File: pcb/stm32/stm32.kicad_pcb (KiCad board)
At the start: 2 copper layers, 57 parts, among them J1 Conn_01x02_Pin, J10 4P4C, J11 4P4C, J12 4P4C, J13 Conn_01x02_Pin, J14 4P4C, J15 4P4C, J16 USB_C_Receptacle, J2 Conn_01x02_Pin, J3 Conn_02x05_Top_Bottom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

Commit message: PCB updates
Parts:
- added Q2: DMG3415, Package_TO_SOT_SMD:SOT-23, F.Cu at (215.0, 53.3)
- added U10: TPL5110, Package_TO_SOT_SMD:SOT-23-6, F.Cu at (215.1, 48.9)
- moved BT1 5.80 mm to (116.8, 40.6)

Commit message: PCB in progress
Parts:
- moved J9 151.8 mm to (50.8, 137.2)
- moved U6 147.4 mm to (72.2, 52.7)
- moved Q1 144.0 mm to (74.6, 61.9)
- moved F1 140.7 mm to (66.0, 63.5)
- moved L1 136.9 mm to (72.2, 47.8)
- moved J10 130.6 mm to (68.7, 137.2)
- moved C7 125.1 mm to (69.4, 53.2), turned to -90 degrees
- moved R14 116.6 mm to (91.4, 33.0)
- moved J16 113.4 mm to (61.0, 81.3), turned to -90 degrees
- moved U8 112.9 mm to (70.0, 82.9)
- moved U9 111.6 mm to (71.8, 78.1)
- moved R15 108.5 mm to (94.0, 38.1)
- moved J11 106.8 mm to (86.9, 137.2)
- moved U4 102.9 mm to (132.1, 71.1)
- moved J12 83.2 mm to (104.6, 136.9)
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
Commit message: Progress
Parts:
- moved C1 173.1 mm to (84.2, 40.6)
- moved U7 154.8 mm to (87.9, 104.0)
- moved U5 153.8 mm to (53.3, 116.8)
- moved J13 142.4 mm to (76.2, 33.6)
- moved U3 129.5 mm to (114.3, 101.6)
- moved C2 122.6 mm to (121.0, 106.7)
- moved C3 117.3 mm to (126.0, 106.7)
- moved C8 115.0 mm to (78.7, 63.5), turned to 90 degrees
- moved Q2 112.7 mm to (102.6, 61.9)
- moved U10 112.7 mm to (102.7, 57.5)
- moved R11 104.0 mm to (100.1, 35.6)
- moved C10 97.4 mm to (105.7, 36.0)
- moved C9 97.4 mm to (105.7, 33.0)
- moved R12 78.0 mm to (120.5, 70.4)
- moved R13 78.0 mm to (120.5, 73.7)
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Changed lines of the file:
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@@
   )
   (footprint "Resistor_SMD:R_1206_3216Metric" (layer "F.Cu")
-    (at 198.44 72.87)
+    (at 120.4575 70.37)
     (descr "Resistor SMD 1206 (3216 Metric), square (rectangular) end terminal, IPC_7351 nominal, (Body size source: IPC-SM-782 page 72, https://www.pcb-3d.com/wordpress/wp-content/uploads/ipc-sm-782a_amendment_1_and_2.pdf), generated with kicad-footprint-generator")
     (tags "resistor")
@@
   )
   (footprint "Capacitor_SMD:C_0805_2012Metric" (layer "F.Cu")
-    (at 243.03 95.39)
+    (at 120.97 106.68)
     (descr "Capacitor SMD 0805 (2012 Metric), square (rectangular) end terminal, IPC_7351 nominal, (Body size source: IPC-SM-782 page 76, https://www.pcb-3d.com/wordpress/wp-content/uploads/ipc-sm-782a_amendment_1_and_2.pdf, https://docs.google.com/spreadsheets/d/1BsfQQcO9C6DZCsRaXUlFlo91Tg2WpOkGARC1WS5S8t0/edit?usp=sharing), generated with kicad-footprint-generator")
     (tags "capacitor")
@@
   )
   (footprint "Package_TO_SOT_SMD:SOT-23" (layer "F.Cu")
-    (at 74.5975 61.91)
+    (at 74.5975 63.5)
     (descr "SOT, 3 Pin (https://www.jedec.org/system/files/docs/to-236h.pdf variant AB), generated with kicad-footprint-generator ipc_gullwing_generator.py")
     (tags "SOT TO_SOT_SMD")
@@
   )
   (footprint "Capacitor_SMD:C_0805_2012Metric" (layer "F.Cu")
-    (at 243.03 98.4)
+    (at 126.05 106.68)
     (descr "Capacitor SMD 0805 (2012 Metric), square (rectangular) end terminal, IPC_7351 nominal, (Body size source: IPC-SM-782 page 76, https://www.pcb-3d.com/wordpress/wp-content/uploads/ipc-sm-782a_amendment_1_and_2.pdf, https://docs.google.com/spreadsheets/d/1BsfQQcO9C6DZCsRaXUlFlo91Tg2WpOkGARC1WS5S8t0/edit?usp=sharing), generated with kicad-footprint-generator")
     (tags "capacitor")
@@
   )
   (footprint "Package_TO_SOT_SMD:SOT-23" (layer "F.Cu")
-    (at 214.9625 53.34)
+    (at 102.6075 61.92)
     (descr "SOT, 3 Pin (https://www.jedec.org/system/files/docs/to-236h.pdf variant AB), generated with kicad-footprint-generator ipc_gullwing_generator.py")
     (tags "SOT TO_SOT_SMD")
@@
   )
   (footprint "Capacitor_SMD:C_0805_2012Metric" (layer "F.Cu")
-    (at 193.41 72.45)
+    (at 78.74 63.5 90)
     (descr "Capacitor SMD 0805 (2012 Metric), square (rectangular) end terminal, IPC_7351 nominal, (Body size source: IPC-SM-782 page 76, https://www.pcb-3d.com/wordpress/wp-content/uploads/ipc-sm-782a_amendment_1_and_2.pdf, https://docs.google.com/spreadsheets/d/1BsfQQcO9C6DZCsRaXUlFlo91Tg2WpOkGARC1WS5S8t0/edit?usp=sharing), generated with kicad-footprint-generator")
     (tags "capacitor")
@@
     (property "ki_keywords" "cap capacitor")
     (attr smd)
-    (fp_text reference "C8" (at 0 -1.68) (layer "F.SilkS")
+    (fp_text reference "C8" (at 2.54 0 180) (layer "F.SilkS")
         (effects (font (size 1 1) (thickness 0.15)))
     )
-    (fp_text value "10u" (at 0 1.68) (layer "F.Fab")
+    (fp_text value "10u" (at -2.54 0 180) (layer "F.Fab")
         (effects (font (size 1 1) (thickness 0.15)))
     )
-    (fp_text user "${REFERENCE}" (at 0 0) (layer "F.Fab")
+    (fp_text user "${REFERENCE}" (at 0 0 90) (layer "F.Fab")
         (effects (font (size 0.5 0.5) (thickness 0.08)))
     )
@@
     (fp_line (start 1 0.625) (end -1 0.625)
       (stroke (width 0.1) (type solid)) (layer "F.Fab"))
-    (pad "1" smd roundrect (at -0.95 0) (size 1 1.45) (layers "F.Cu" "F.Paste" "F.Mask") (roundrect_rratio 0.25)
+    (pad "1" smd roundrect (at -0.95 0 90) (size 1 1.45) (layers "F.Cu" "F.Paste" "F.Mask") (roundrect_rratio 0.25)
       (net 3 "+3.3V") (pintype "passive"))
-    (pad "2" smd roundrect (at 0.95 0) (size 1 1.45) (layers "F.Cu" "F.Paste" "F.Mask") (roundrect_rratio 0.25)
+    (pad "2" smd roundrect (at 0.95 0 90) (size 1 1.45) (layers "F.Cu" "F.Paste" "F.Mask") (roundrect_rratio 0.25)
       (net 2 "GND") (pintype "passive"))
     (model "${KICAD6_3DMODEL_DIR}/Capacitor_SMD.3dshapes/C_0805_2012Metric.wrl"
@@
   )
   (footprint "Connector_PinHeader_2.00mm:PinHeader_1x02_P2.00mm_Vertical" (layer "F.Cu")
-    (at 213.88 69.96)
+    (at 76.2 33.56)
     (descr "Through hole straight pin header, 1x02, 2.00mm pitch, single row")
     (tags "Through hole pin header THT 1x02 2.00mm single row")
@@
   )
   (footprint "Capacitor_SMD:C_0805_2012Metric" (layer "F.Cu")
-    (at 193.41 75.46)
+    (at 105.73 33.02)
     (descr "Capacitor SMD 0805 (2012 Metric), square (rectangular) end terminal, IPC_7351 nominal, (Body size source: IPC-SM-782 page 76, https://www.pcb-3d.com/wordpress/wp-content/uploads/ipc-sm-782a_amendment_1_and_2.pdf, https://docs.google.com/spreadsheets/d/1BsfQQcO9C6DZCsRaXUlFlo91Tg2WpOkGARC1WS5S8t0/edit?usp=sharing), generated with kicad-footprint-generator")
     (tags "capacitor")
@@
   )
   (footprint "Capacitor_SMD:C_0805_2012Metric" (layer "F.Cu")
-    (at 193.41 78.47)
+    (at 105.73 36.03)
     (descr "Capacitor SMD 0805 (2012 Metric), square (rectangular) end terminal, IPC_7351 nominal, (Body size source: IPC-SM-782 page 76, https://www.pcb-3d.com/wordpress/wp-content/uploads/ipc-sm-782a_amendment_1_and_2.pdf, https://docs.google.com/spreadsheets/d/1BsfQQcO9C6DZCsRaXUlFlo91Tg2WpOkGARC1WS5S8t0/edit?usp=sharing), generated with kicad-footprint-generator")
     (tags "capacitor")
@@
   )
   (footprint "Package_TO_SOT_SMD:SOT-23-5" (layer "F.Cu")
-    (at 243.38 91.66)
+    (at 114.3 101.6)
     (descr "SOT, 5 Pin (https://www.jedec.org/sites/default/files/docs/Mo-178c.PDF variant AA), generated with kicad-footprint-generator ipc_gullwing_generator.py")
     (tags "SOT TO_SOT_SMD")
@@
   )
   (footprint "Package_LGA:Bosch_LGA-8_2.5x2.5mm_P0.65mm_ClockwisePinNumbering" (layer "F.Cu")
-    (at 242.74 103.97)
+    (at 87.925 103.97)
     (descr "LGA-8")
     (tags "lga land grid array")
@@
   )
   (footprint "Package_TO_SOT_SMD:SOT-23-5" (layer "F.Cu")
-    (at 243.38 87.21)
+    (at 247.5175 54.29)
     (descr "SOT, 5 Pin (https://www.jedec.org/sites/default/files/docs/Mo-178c.PDF variant AA), generated with kicad-footprint-generator ipc_gullwing_generator.py")
     (tags "SOT TO_SOT_SMD")
@@
   )
   (footprint "Capacitor_SMD:C_0201_0603Metric" (layer "F.Cu")
-    (at 247.18 98.89)
+    (at 84.165 40.64)
     (descr "Capacitor SMD 0201 (0603 Metric), square (rectangular) end terminal, IPC_7351 nominal, (Body size source: https://www.vishay.com/docs/20052/crcw0201e3.pdf), generated with kicad-footprint-generator")
     (tags "capacitor")
@@
   )
   (footprint "Resistor_SMD:R_1206_3216Metric" (layer "F.Cu")
-    (at 198.44 76.16)
+    (at 120.4575 73.66)
     (descr "Resistor SMD 1206 (3216 Metric), square (rectangular) end terminal, IPC_7351 nominal, (Body size source: IPC-SM-782 page 72, https://www.pcb-3d.com/wordpress/wp-content/uploads/ipc-sm-782a_amendment_1_and_2.pdf), generated with kicad-footprint-generator")
     (tags "resistor")
@@
   )
   (footprint "Package_SO:SOIC-8_3.9x4.9mm_P1.27mm" (layer "F.Cu")
-    (at 250.18 88.21)
+    (at 254.3175 55.29)
     (descr "SOIC, 8 Pin (JEDEC MS-012AA, https://www.analog.com/media/en/package-pcb-resources/package/pkg_pdf/soic_narrow-r/r_8.pdf), generated with kicad-footprint-generator ipc_gullwing_generator.py")
     (tags "SOIC SO")
@@
   )
   (footprint "Package_TO_SOT_SMD:SOT-23-6" (layer "F.Cu")
-    (at 215.0925 48.89)
+    (at 102.7375 57.47)
     (descr "SOT, 6 Pin (https://www.jedec.org/sites/default/files/docs/Mo-178c.PDF variant AB), generated with kicad-footprint-generator ipc_gullwing_generator.py")
     (tags "SOT TO_SOT_SMD")
@@
   )
   (footprint "Resistor_SMD:R_1206_3216Metric" (layer "F.Cu")
-    (at 198.44 69.58)
+    (at 100.1375 35.56)
     (descr "Resistor SMD 1206 (3216 Metric), square (rectangular) end terminal, IPC_7351 nominal, (Body size source: IPC-SM-782 page 72, https://www.pcb-3d.com/wordpress/wp-content/uploads/ipc-sm-782a_amendment_1_and_2.pdf), generated with kicad-footprint-generator")
     (tags "resistor")
@@
   )
   (footprint "Package_TO_SOT_THT:TO-92_Inline" (layer "F.Cu")
-    (at 184.66 36.71)
+    (at 53.34 116.84)
     (descr "TO-92 leads in-line, narrow, oval pads, drill 0.75mm (see NXP sot054_po.pdf)")
     (tags "to-92 sc-43 sc-43a sot54 PA33 transistor")

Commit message: Setup board
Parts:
- moved U9 3.63 mm to (74.3, 75.5)
- moved U8 3.63 mm to (72.5, 80.2)
- moved J16 2.64 mm to (61.0, 78.6)
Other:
- board outline added: 99.1 x 50.8 mm
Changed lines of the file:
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@@
   )
   (setup
+    (stackup
+      (layer "F.SilkS" (type "Top Silk Screen"))
+      (layer "F.Paste" (type "Top Solder Paste"))
+      (layer "F.Mask" (type "Top Solder Mask") (thickness 0.01))
+      (layer "F.Cu" (type "copper") (thickness 0.035))
+      (layer "dielectric 1" (type "core") (thickness 1.51) (material "FR4") (epsilon_r 4.5) (loss_tangent 0.02))
+      (layer "B.Cu" (type "copper") (thickness 0.035))
+      (layer "B.Mask" (type "Bottom Solder Mask") (thickness 0.01))
+      (layer "B.Paste" (type "Bottom Solder Paste"))
+      (layer "B.SilkS" (type "Bottom Silk Screen"))
+      (copper_finish "HAL SnPb")
+      (dielectric_constraints no)
+    )
     (pad_to_mask_clearance 0)
     (pcbplotparams
@@
   )
   (footprint "Package_TO_SOT_SMD:SOT-23-6" (layer "F.Cu")
-    (at 69.9825 82.87)
+    (at 72.475 80.23)
     (descr "SOT, 6 Pin (https://www.jedec.org/sites/default/files/docs/Mo-178c.PDF variant AB), generated with kicad-footprint-generator ipc_gullwing_generator.py")
     (tags "SOT TO_SOT_SMD")
@@
   )
   (footprint "Connector_USB:USB_C_Receptacle_Amphenol_12401548E4-2A" (layer "F.Cu")
-    (at 60.96 81.28 -90)
+    (at 60.96 78.64 -90)
     (descr "USB TYPE C, RA RCPT PCB, Hybrid, https://www.amphenolcanada.com/StockAvailabilityPrice.aspx?From=&PartNum=12401548E4%7e2A")
     (tags "USB C Type-C Receptacle Hybrid")
@@
   )
   (footprint "Package_DFN_QFN:QFN-24-1EP_4x4mm_P0.5mm_EP2.6x2.6mm" (layer "F.Cu")
-    (at 71.77 78.09)
+    (at 74.2625 75.45)
     (descr "QFN, 24 Pin (http://ww1.microchip.com/downloads/en/PackagingSpec/00000049BQ.pdf#page=278), generated with kicad-footprint-generator ipc_noLead_generator.py")
     (tags "QFN NoLead")
@@
     )
   )
+  (gr_rect (start 55.88 38.1) (end 154.94 88.9)
+    (stroke (width 0.1) (type default)) (fill none) (layer "Edge.Cuts"))
 )

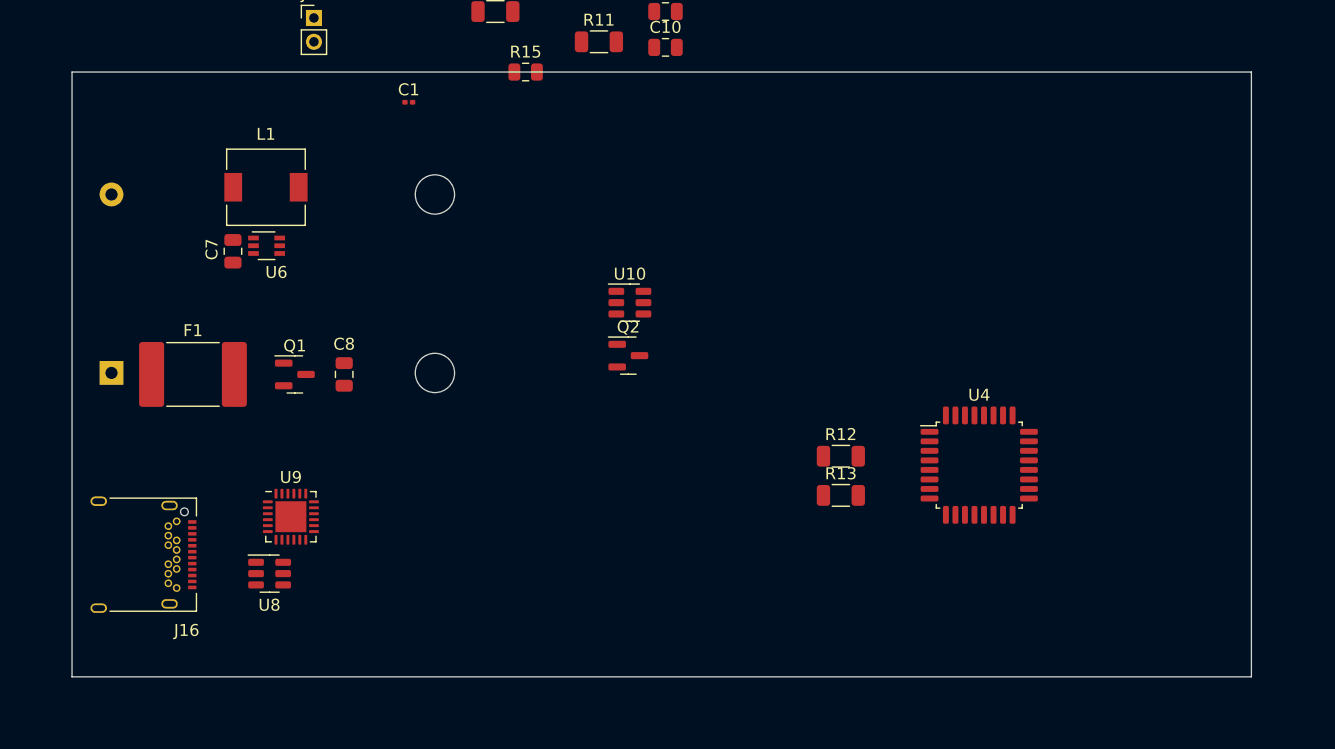
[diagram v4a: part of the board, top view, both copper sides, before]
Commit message: Updated tracks in PCB
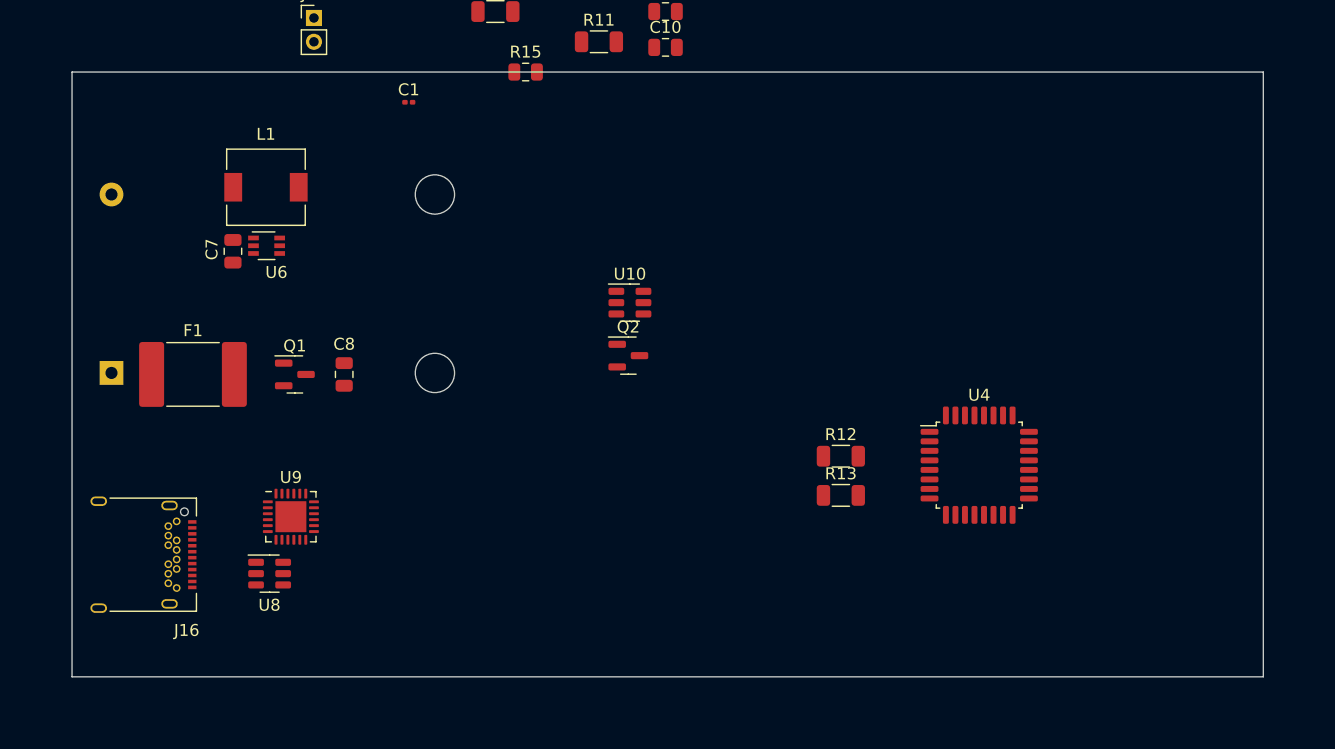
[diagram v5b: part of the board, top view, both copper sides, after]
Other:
- board size 99.1 x 50.8 mm -> 100.1 x 50.8 mm
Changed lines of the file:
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@@
     )
   )
-  (gr_rect (start 55.88 38.1) (end 154.94 88.9)
+  (gr_rect (start 55.88 38.1) (end 155.94 88.9)
     (stroke (width 0.1) (type default)) (fill none) (layer "Edge.Cuts"))
 )

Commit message: Small work on pcb
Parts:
- moved U5 159.5 mm to (211.0, 141.0)
- moved U7 139.1 mm to (222.0, 141.0)
- moved C2 138.8 mm to (255.0, 143.0)
- moved C3 138.8 mm to (260.1, 143.0)
- moved U3 138.8 mm to (248.3, 137.9)
- moved J1 133.8 mm to (124.0, 60.0)
- moved J14 114.3 mm to (130.9, 25.4), turned to 180 degrees
- moved J15 112.6 mm to (147.5, 25.2), turned to 180 degrees
- moved C4 101.8 mm to (159.7, 43.0)
- moved J9 99.5 mm to (143.9, 102.0), turned to 180 degrees
- moved C5 88.1 mm to (162.7, 63.0)
- moved SW1 87.0 mm to (149.9, 65.9)
- moved C6 86.5 mm to (167.1, 57.0)
- moved SW2 82.8 mm to (150.1, 73.1)
- moved SW3 82.0 mm to (150.0, 80.0)
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
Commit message: update
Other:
- board text added: "TODO: breadboard"
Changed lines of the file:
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@@
   (gr_rect (start 55.88 38.1) (end 155.94 88.9)
     (stroke (width 0.1) (type default)) (fill none) (layer "Edge.Cuts"))
+  (gr_text "TODO: breadboard\n" (at 129.54 121.92) (layer "F.SilkS")
+    (effects (font (size 1.5 1.5) (thickness 0.3) bold) (justify left bottom))
+  )
 )
